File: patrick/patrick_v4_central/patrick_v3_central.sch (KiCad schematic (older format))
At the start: 14 parts, among them J1 Conn_02x05_Counter_Clockwise, J10 61300311121, J2 Conn_02x05_Counter_Clockwise, J3 Conn_02x05_Counter_Clockwise, J4 Conn_02x05_Counter_Clockwise, J5 Conn_02x05_Counter_Clockwise, J7 61300211121, J9 61300211121, U3 BL652-SA-01

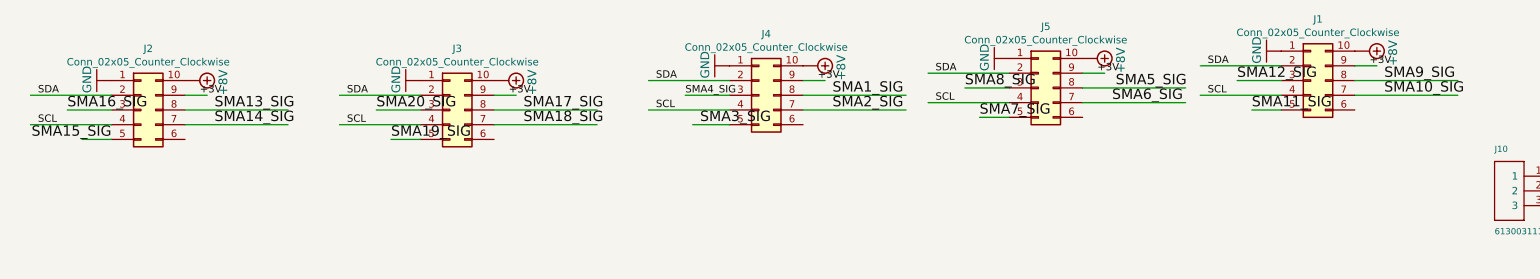
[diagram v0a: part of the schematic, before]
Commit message: added IMU to 3 legged circuit
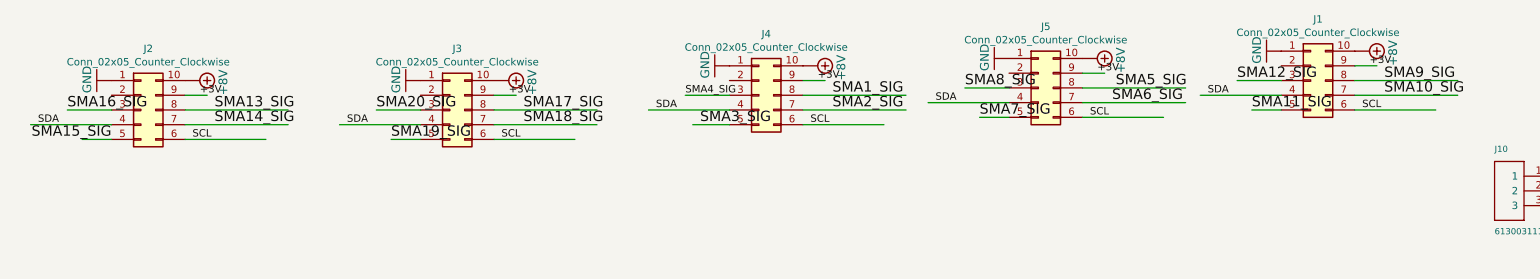
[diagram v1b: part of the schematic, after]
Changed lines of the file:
@@
 +3V
 Wire Wire Line
+	2850 3150 2300 3150
+Wire Wire Line
 	1800 3050 1250 3050
-Wire Wire Line
-	1800 2850 1250 2850
+Text Label 2350 3150 0    50   ~ 0
+SCL
 Text Label 1300 3050 0    50   ~ 0
-SCL
-Text Label 1300 2850 0    50   ~ 0
 SDA
 Wire Wire Line
+	4950 3150 4400 3150
+Wire Wire Line
 	3900 3050 3350 3050
-Wire Wire Line
-	3900 2850 3350 2850
+Text Label 4450 3150 0    50   ~ 0
+SCL
 Text Label 3400 3050 0    50   ~ 0
-SCL
-Text Label 3400 2850 0    50   ~ 0
 SDA
 Wire Wire Line
+	7050 3050 6500 3050
+Wire Wire Line
 	6000 2950 5450 2950
-Wire Wire Line
-	6000 2750 5450 2750
-Text Label 5500 2750 0    50   ~ 0
+Text Label 5500 2950 0    50   ~ 0
 SDA
 Wire Wire Line
+	8950 3000 8400 3000
+Wire Wire Line
 	7900 2900 7350 2900
-Wire Wire Line
-	7900 2700 7350 2700
+Text Label 8450 3000 0    50   ~ 0
+SCL
 Text Label 7400 2900 0    50   ~ 0
-SCL
-Text Label 7400 2700 0    50   ~ 0
 SDA
 Wire Wire Line
+	10800 2950 10250 2950
+Wire Wire Line
 	9750 2850 9200 2850
-Wire Wire Line
-	9750 2650 9200 2650
+Text Label 10300 2950 0    50   ~ 0
+SCL
 Text Label 9250 2850 0    50   ~ 0
-SCL
-Text Label 9250 2650 0    50   ~ 0
 SDA
 Wire Wire Line
@@
 Wire Wire Line
 	15000 6550 15000 6800
-Text Label 5500 2950 0    50   ~ 0
+Text Label 6550 3050 0    50   ~ 0
 SCL
 Wire Wire Line
